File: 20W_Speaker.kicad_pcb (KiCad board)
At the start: 2 copper layers, 26.7 x 19.3 mm, 24 parts, among them J1 Conn_01x02, J2 Conn_01x02, J3 Conn_01x02, J4 Conn_01x02, U1 PAM8320RDR

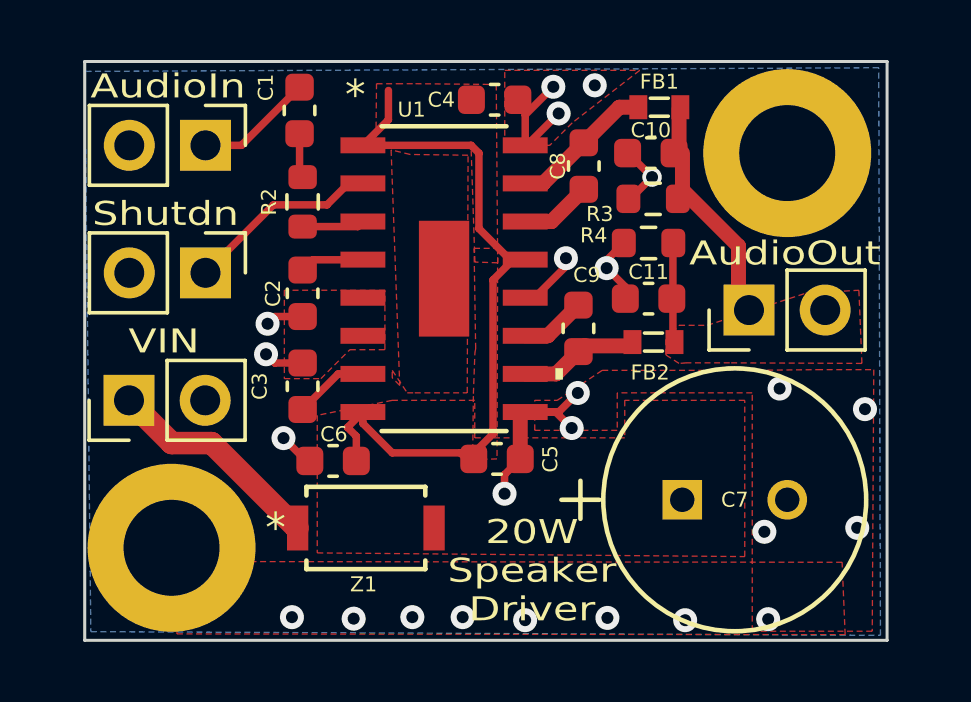
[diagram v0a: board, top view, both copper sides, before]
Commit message: PCB submitted for order
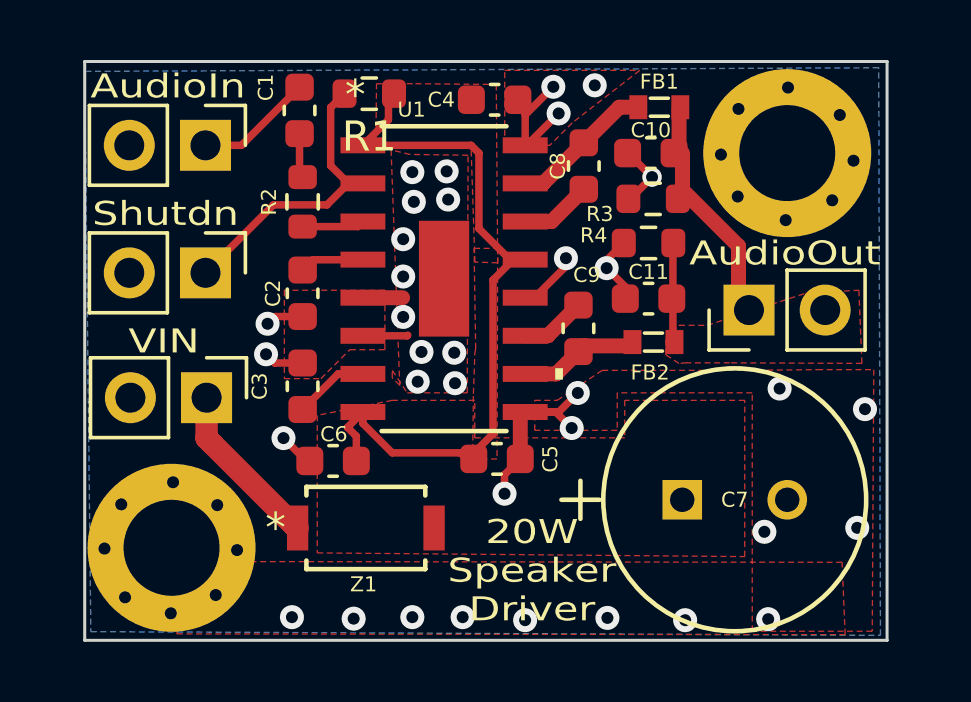
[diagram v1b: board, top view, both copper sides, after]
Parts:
- added R1: 4.7k, Resistor_SMD:R_0603_1608Metric, F.Cu at (152.2, 84.3)
- moved J2 2.59 mm to (146.8, 94.4), turned to -90 degrees
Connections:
- U1 pad 17: unconnected-(U1-EPAD-Pad17) -> GND
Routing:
- net GND: track 20.9 -> 25.4 mm, vias 24 -> 51
- net Net-(J1-Pin_1): track 6.48 -> 9.91 mm
- net Net-(J2-Pin_1): track 7.38 -> 5.72 mm
- removed copper zone on F.Cu, net unconnected-(U1-EPAD-Pad17)
